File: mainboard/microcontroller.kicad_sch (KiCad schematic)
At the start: 22 parts, among them SW1 SW_SPST, SW2 SW_SPST, U2 W25Q16JVUXIQ TR, U7 RP2040, Y1 12MHz

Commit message: Prepared for PCB layout
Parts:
- R17, R18: DPN (none) -> RMCF0603FT10K0CT-ND; MPN (none) -> RMCF0603FT10K0
- SW1, SW2: footprint BreadboardBuddy:SW_SPST_3.3x3.1 -> lib:SW_SPST_3.3x3.1
- U2: footprint BreadboardBuddy:8-UFDFN -> lib:8-UFDFN
- U7: DPN (none) -> 2648-SC0914(13)CT-ND; MPN (none) -> SC0914(13)
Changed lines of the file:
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@@
 			)
 		)
-		(property "Footprint" "BreadboardBuddy:SW_SPST_3.3x3.1"
+		(property "Footprint" "lib:SW_SPST_3.3x3.1"
 			(at 109.22 68.58 0)
 			(effects
@@
 			)
 		)
+		(property "DPN" "RMCF0603FT10K0CT-ND"
+			(at 218.44 138.43 0)
+			(effects
+				(font
+					(size 1.27 1.27)
+				)
+				(hide yes)
+			)
+		)
+		(property "MPN" "RMCF0603FT10K0"
+			(at 218.44 138.43 0)
+			(effects
+				(font
+					(size 1.27 1.27)
+				)
+				(hide yes)
+			)
+		)
 		(pin "2"
 		)
@@
 			)
 		)
+		(property "DPN" "2648-SC0914(13)CT-ND"
+			(at 157.48 106.68 0)
+			(effects
+				(font
+					(size 1.27 1.27)
+				)
+				(hide yes)
+			)
+		)
+		(property "MPN" "SC0914(13)"
+			(at 157.48 106.68 0)
+			(effects
+				(font
+					(size 1.27 1.27)
+				)
+				(hide yes)
+			)
+		)
 		(pin "19"
 		)
@@
 			)
 		)
-		(property "Footprint" "BreadboardBuddy:SW_SPST_3.3x3.1"
+		(property "Footprint" "lib:SW_SPST_3.3x3.1"
 			(at 63.5 127 0)
 			(effects
@@
 			)
 		)
-		(property "Footprint" "BreadboardBuddy:8-UFDFN"
+		(property "Footprint" "lib:8-UFDFN"
 			(at 73.66 106.68 0)
 			(effects
@@
 			(at 218.44 148.59 0)
 			(effects
+				(font
+					(size 1.27 1.27)
+				)
+				(hide yes)
+			)
+		)
+		(property "DPN" "RMCF0603FT10K0CT-ND"
+			(at 218.44 148.59 0)
+			(effects
+				(font
+					(size 1.27 1.27)
+				)
+				(hide yes)
+			)
+		)
+		(property "MPN" "RMCF0603FT10K0"
+			(at 218.44 148.59 0)
+			(effects

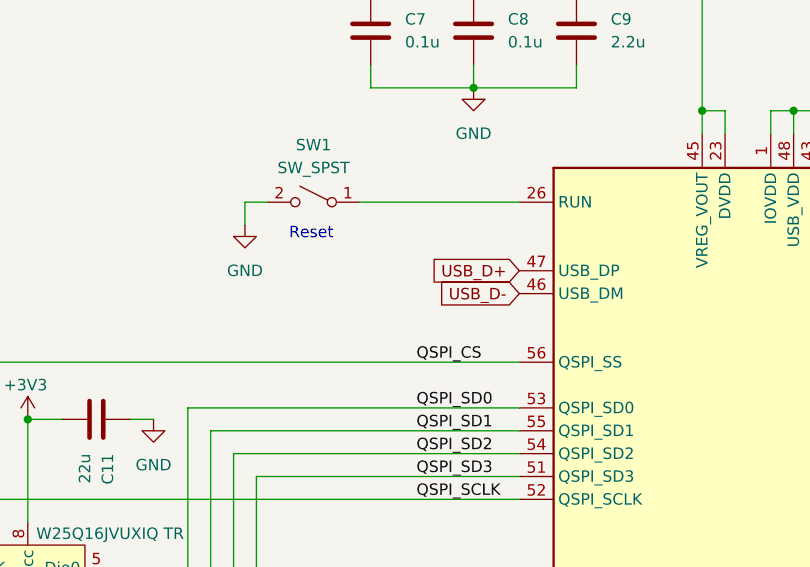
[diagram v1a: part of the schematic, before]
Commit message: Added some 3d libs and started routing
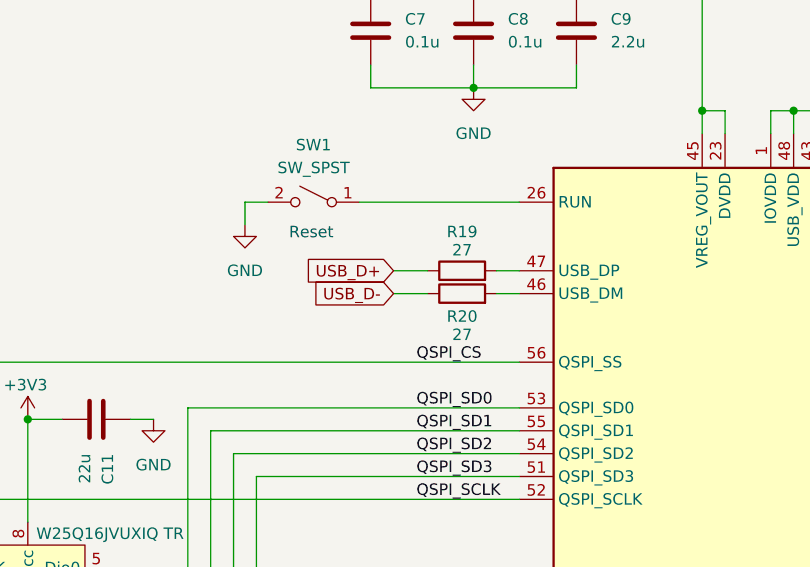
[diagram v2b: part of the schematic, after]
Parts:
- added R19, R20: 27, Resistor_SMD:R_0603_1608Metric, symbol Device:R
- SW1, SW2: footprint lib:SW_SPST_3.3x3.1 -> lib:SW_SPST_2.8x1.9
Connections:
- net USB_D+: now also R19.1; no longer U7.47 (USB_DP)
- net USB_D-: now also R20.1; no longer U7.46 (USB_DM)
- new net: R20.2, U7.46 (USB_DM)
- new net: R19.2, U7.47 (USB_DP)
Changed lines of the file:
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@@
+	(wire
+		(pts
+			(xy 121.92 78.74) (xy 118.11 78.74)
+		)
+		(stroke
+			(width 0)
+			(type default)
+		)
+	)
 	(wire
 		(pts
@@
 	(wire
 		(pts
+			(xy 129.54 76.2) (xy 132.08 76.2)
+		)
+		(stroke
+			(width 0)
+			(type default)
+		)
+	)
+	(wire
+		(pts
 			(xy 160.02 60.96) (xy 160.02 58.42)
 		)
@@
 	(wire
 		(pts
+			(xy 121.92 76.2) (xy 118.11 76.2)
+		)
+		(stroke
+			(width 0)
+			(type default)
+		)
+	)
+	(wire
+		(pts
 			(xy 201.93 137.16) (xy 201.93 143.51)
 		)
@@
 		(pts
 			(xy 101.6 68.58) (xy 101.6 71.12)
+		)
+		(stroke
+			(width 0)
+			(type default)
+		)
+	)
+	(wire
+		(pts
+			(xy 129.54 78.74) (xy 132.08 78.74)
 		)
 		(stroke
@@
 	(global_label "USB_D+"
 		(shape input)
-		(at 132.08 76.2 180)
+		(at 118.11 76.2 180)
 		(fields_autoplaced yes)
 		(effects
@@
 		)
 		(property "Intersheetrefs" "${INTERSHEET_REFS}"
-			(at 121.5542 76.2 0)
+			(at 107.5842 76.2 0)
 			(effects
 				(font
@@
 	(global_label "USB_D-"
 		(shape input)
-		(at 132.08 78.74 180)
+		(at 118.11 78.74 180)
 		(fields_autoplaced yes)
 		(effects
@@
 		)
 		(property "Intersheetrefs" "${INTERSHEET_REFS}"
-			(at 121.5542 78.74 0)
+			(at 107.5842 78.74 0)
 			(effects
 				(font
@@
 				(path "/710151bd-e30e-4e9c-b9ee-6f0d49a79794/eadbe4be-210b-427d-b66a-812f3e0066c9"
 					(reference "#PWR048")
+					(unit 1)
+				)
+			)
+		)
+	)
+	(symbol
+		(lib_id "Device:R")
+		(at 125.73 78.74 90)
+		(unit 1)
+		(exclude_from_sim no)
+		(in_bom yes)
+		(on_board yes)
+		(dnp no)
+		(property "Reference" "R20"
+			(at 125.73 81.28 90)
+			(effects
+				(font
+					(size 1.27 1.27)
+				)
+			)
+		)
+		(property "Value" "27"
+			(at 125.73 83.312 90)
+			(effects
+				(font
+					(size 1.27 1.27)
+				)
+			)
+		)
+		(property "Footprint" "Resistor_SMD:R_0603_1608Metric"
+			(at 125.73 80.518 90)
+			(effects
+				(font
+					(size 1.27 1.27)
+				)
+				(hide yes)
+			)
+		)
+		(property "Datasheet" "~"
+			(at 125.73 78.74 0)
+			(effects
+				(font
+					(size 1.27 1.27)
+				)
+				(hide yes)
+			)
+		)
+		(property "Description" "Resistor"
+			(at 125.73 78.74 0)
+			(effects
+				(font
+					(size 1.27 1.27)
+				)
+				(hide yes)
+			)
+		)
+		(property "DPN" "CR0603-FX-27R0ELFCT-ND"
+			(at 125.73 78.74 0)
+			(effects
+				(font
+					(size 1.27 1.27)
+				)
+				(hide yes)
+			)
+		)
+		(property "MPN" "CR0603-FX-27R0ELF"
+			(at 125.73 78.74 0)
+			(effects
+				(font
+					(size 1.27 1.27)
+				)
+				(hide yes)
+			)
+		)
+		(pin "2"
+		)
+		(pin "1"
+		)
+		(instances
+			(project "mainboard"
+				(path "/710151bd-e30e-4e9c-b9ee-6f0d49a79794/eadbe4be-210b-427d-b66a-812f3e0066c9"
+					(reference "R20")
 					(unit 1)
 				)
@@
 			)
 		)
-		(property "Footprint" "lib:SW_SPST_3.3x3.1"
+		(property "Footprint" "lib:SW_SPST_2.8x1.9"
 			(at 109.22 68.58 0)
 			(effects
@@
 	)
 	(symbol
+		(lib_id "Device:R")
+		(at 125.73 76.2 90)
+		(unit 1)
+		(exclude_from_sim no)
+		(in_bom yes)
+		(on_board yes)
+		(dnp no)
+		(property "Reference" "R19"
+			(at 125.73 71.882 90)
+			(effects
+				(font
+					(size 1.27 1.27)
+				)
+			)
+		)
+		(property "Value" "27"
+			(at 125.73 73.914 90)
+			(effects
+				(font
+					(size 1.27 1.27)
+				)
+			)
+		)
+		(property "Footprint" "Resistor_SMD:R_0603_1608Metric"
+			(at 125.73 77.978 90)
+			(effects
+				(font
+					(size 1.27 1.27)
+				)
+				(hide yes)
+			)
+		)
+		(property "Datasheet" "~"
+			(at 125.73 76.2 0)
+			(effects
+				(font
+					(size 1.27 1.27)
+				)
+				(hide yes)
+			)
+		)
+		(property "Description" "Resistor"
+			(at 125.73 76.2 0)
+			(effects
+				(font
+					(size 1.27 1.27)
+				)
+				(hide yes)
+			)
+		)
+		(property "DPN" "CR0603-FX-27R0ELFCT-ND"
+			(at 125.73 76.2 0)
+			(effects
+				(font
+					(size 1.27 1.27)
+				)
+				(hide yes)
+			)
+		)
+		(property "MPN" "CR0603-FX-27R0ELF"
+			(at 125.73 76.2 0)
+			(effects
+				(font
+					(size 1.27 1.27)
+				)
+				(hide yes)
+			)
+		)
+		(pin "2"
+		)
+		(pin "1"
+		)
+		(instances
+			(project "mainboard"
+				(path "/710151bd-e30e-4e9c-b9ee-6f0d49a79794/eadbe4be-210b-427d-b66a-812f3e0066c9"
+					(reference "R19")
+					(unit 1)
+				)
+			)
+		)
+	)
+	(symbol
 		(lib_id "power:GND")
 		(at 106.68 137.16 0)
@@
 			)
 		)
-		(property "Footprint" "lib:SW_SPST_3.3x3.1"
+		(property "Footprint" "lib:SW_SPST_2.8x1.9"
 			(at 63.5 127 0)
 			(effects

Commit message: More building
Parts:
- added TP7: TestPoint, TestPoint:TestPoint_Pad_D1.0mm, symbol Connector:TestPoint
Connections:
- net at U7.39 (GPIO27_ADC1): now also TP7.1
- no-connect marks 0 -> 19
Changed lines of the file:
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@@
 		(color 0 0 0 0)
+	)
+	(no_connect
+		(at 182.88 99.06)
+	)
+	(no_connect
+		(at 182.88 88.9)
+	)
+	(no_connect
+		(at 182.88 116.84)
+	)
+	(no_connect
+		(at 182.88 142.24)
+	)
+	(no_connect
+		(at 182.88 93.98)
+	)
+	(no_connect
+		(at 182.88 114.3)
+	)
+	(no_connect
+		(at 182.88 106.68)
+	)
+	(no_connect
+		(at 182.88 121.92)
+	)
+	(no_connect
+		(at 182.88 119.38)
+	)
+	(no_connect
+		(at 182.88 104.14)
+	)
+	(no_connect
+		(at 182.88 96.52)
+	)
+	(no_connect
+		(at 182.88 91.44)
+	)
+	(no_connect
+		(at 182.88 144.78)
+	)
+	(no_connect
+		(at 182.88 129.54)
+	)
+	(no_connect
+		(at 182.88 101.6)
+	)
+	(no_connect
+		(at 132.08 137.16)
+	)
+	(no_connect
+		(at 182.88 127)
+	)
+	(no_connect
+		(at 182.88 124.46)
+	)
+	(no_connect
+		(at 132.08 134.62)
 	)
 	(wire
@@
 					(unit 1)
 				)
+			)
+		)
+	)
+	(symbol
+		(lib_id "Connector:TestPoint")
+		(at 182.88 139.7 270)
+		(unit 1)
+		(exclude_from_sim no)
+		(in_bom yes)
+		(on_board yes)
+		(dnp no)
+		(property "Reference" "TP7"
+			(at 189.23 139.7 90)
+			(effects
+				(font
+					(size 1.27 1.27)
+				)
+			)
+		)
+		(property "Value" "TestPoint"
+			(at 186.182 142.24 90)
+			(effects
+				(font
+					(size 1.27 1.27)
+				)
+				(hide yes)
+			)
+		)
+		(property "Footprint" "TestPoint:TestPoint_Pad_D1.0mm"
+			(at 182.88 144.78 0)
+			(effects
+				(font
+					(size 1.27 1.27)
+				)
+				(hide yes)
+			)
+		)
+		(property "Datasheet" "~"
+			(at 182.88 144.78 0)
+			(effects
+				(font
+					(size 1.27 1.27)
+				)
+				(hide yes)
+			)
+		)
+		(property "Description" "test point"
+			(at 182.88 139.7 0)
+			(effects
+				(font
+					(size 1.27 1.27)
+				)
+				(hide yes)
+			)
+		)
+		(pin "1"
+		)
+		(instances
+			(project "mainboard"
+				(path "/710151bd-e30e-4e9c-b9ee-6f0d49a79794/eadbe4be-210b-427d-b66a-812f3e0066c9"
+					(reference "TP7")
+					(unit 1)
+				)

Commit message: Finished routing
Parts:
- added J5, J6: Conn_01x04, Connector_PinHeader_1.00mm:PinHeader_1x04_P1.00mm_Vertical, symbol Connector_Generic:Conn_01x04
- added TP5: TestPoint, TestPoint:TestPoint_Pad_D1.0mm, symbol Connector:TestPoint
- SW1, SW2: DPN 1642-LS38J2F-TCT-ND -> 450-3358-1-ND; MPN LS38J2F-T -> USLPT2819DT2TR
- renumbered TP7 to TP6
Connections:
- net GND: now also SW2.2 (B); no longer SW2.1 (A)
- net QSPI_CS: now also SW2.1 (A); no longer SW2.2 (B)
- net at U7.11 (GPIO8): now also J5.1 (Pin_1)
- net at U7.12 (GPIO9): now also J5.2 (Pin_2)
- net at U7.13 (GPIO10): now also J5.3 (Pin_3)
- net at U7.14 (GPIO11): now also J5.4 (Pin_4)
- net at U7.15 (GPIO12): now also J6.1 (Pin_1)
- net at U7.16 (GPIO13): now also J6.2 (Pin_2)
- net at U7.17 (GPIO14): now also J6.3 (Pin_3)
- net at U7.18 (GPIO15): now also J6.4 (Pin_4)
- net at U7.29 (GPIO18): now also TP5.1
- no-connect marks 19 -> 10
